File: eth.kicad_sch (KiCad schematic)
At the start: 58 parts, among them U1901 KSZ9131RNXC, Y1901 Resonator_25MHz_ECX-1247Q

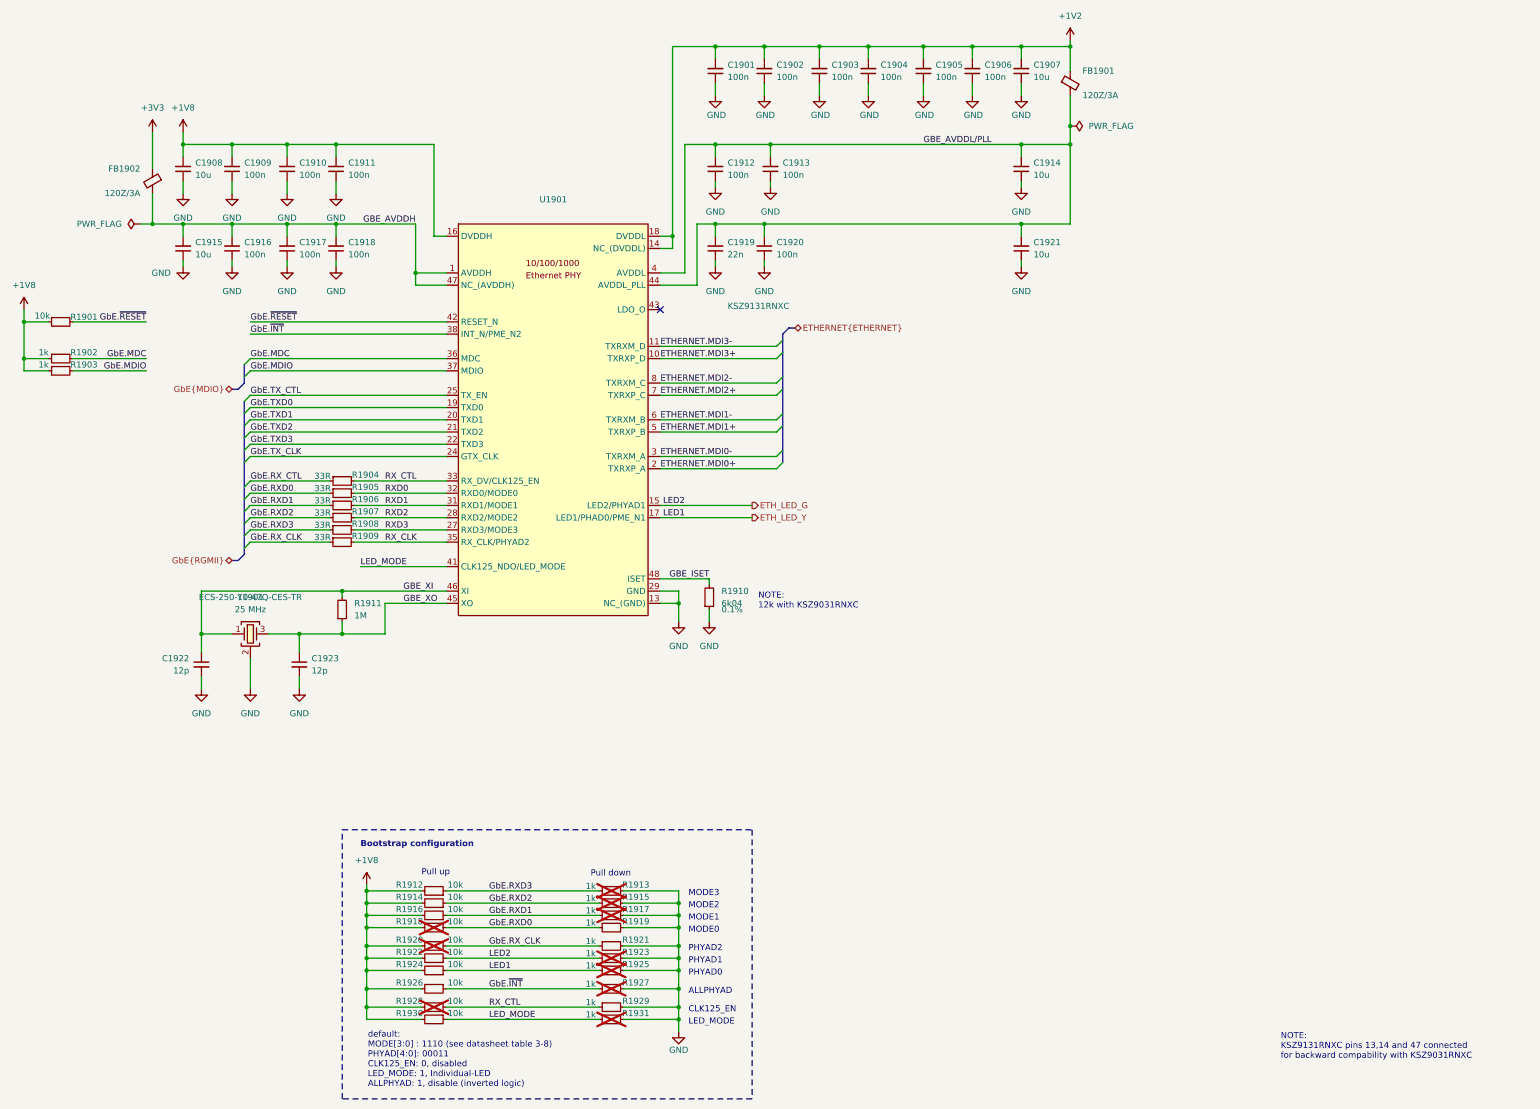
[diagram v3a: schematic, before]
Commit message: [#100282] Clear ERC
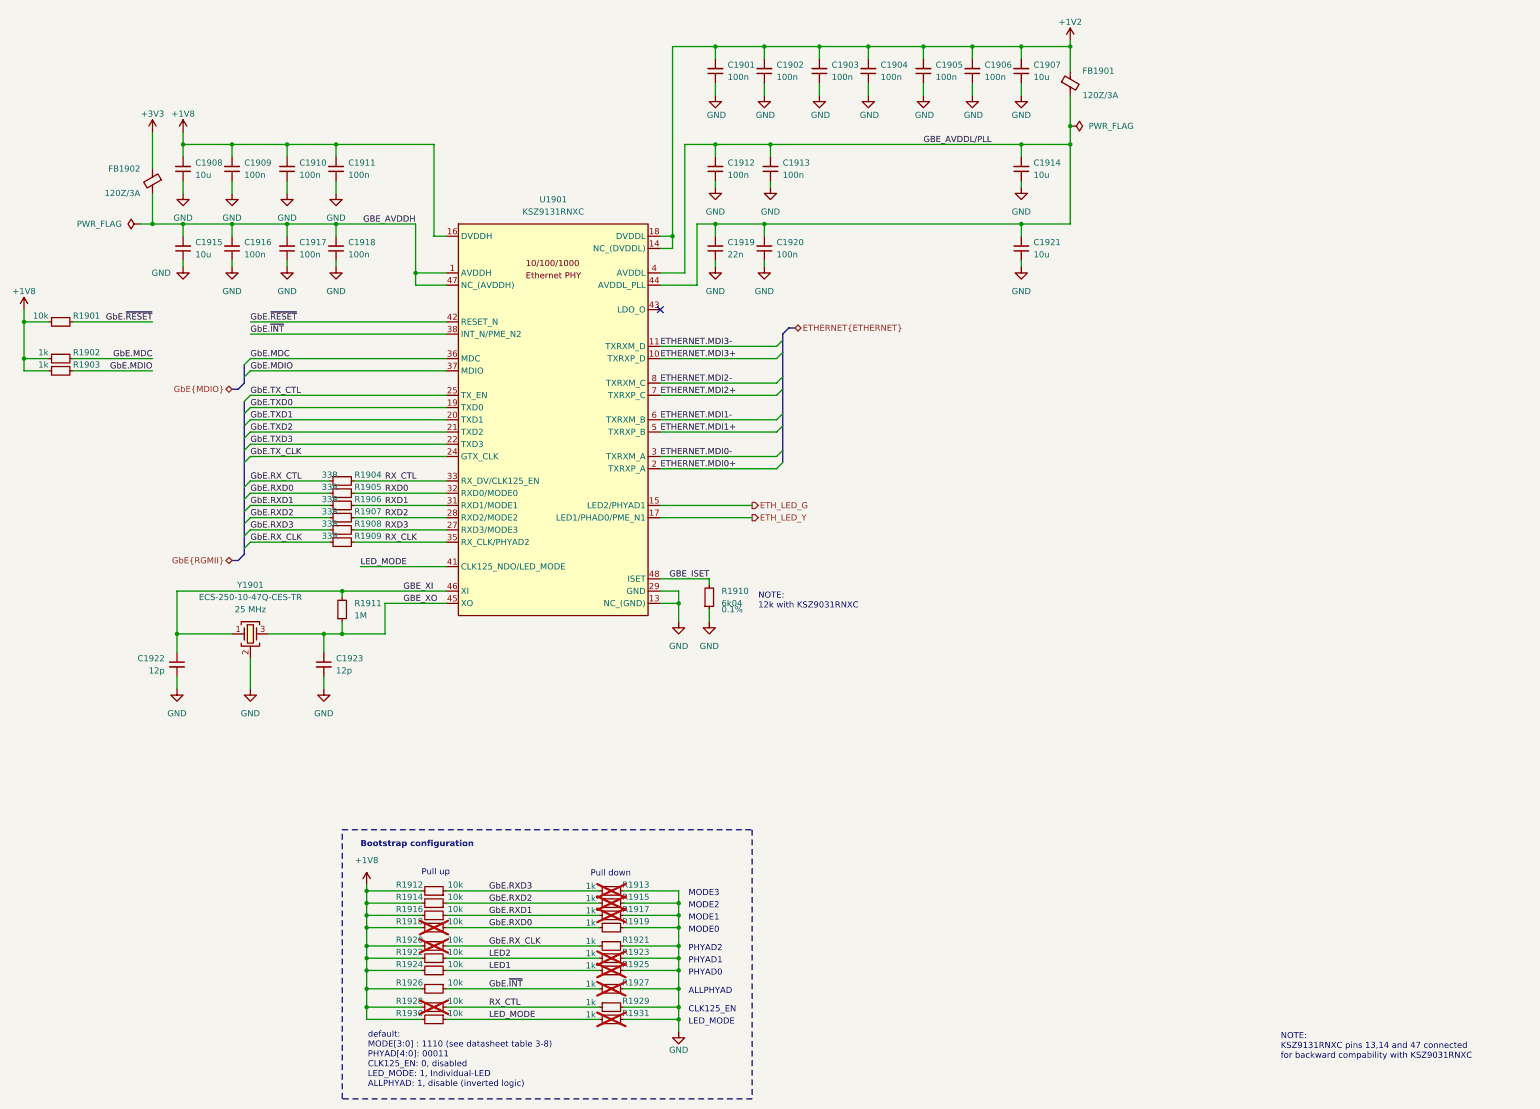
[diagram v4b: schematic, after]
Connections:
- net ETH_LED_G: no longer R1922.1, R1923.1
- net ETH_LED_Y: no longer R1924.1, R1925.1
- new net LED1: R1924.1, R1925.1
- new net LED2: R1922.1, R1923.1
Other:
- moved on the sheet: C1922, C1923

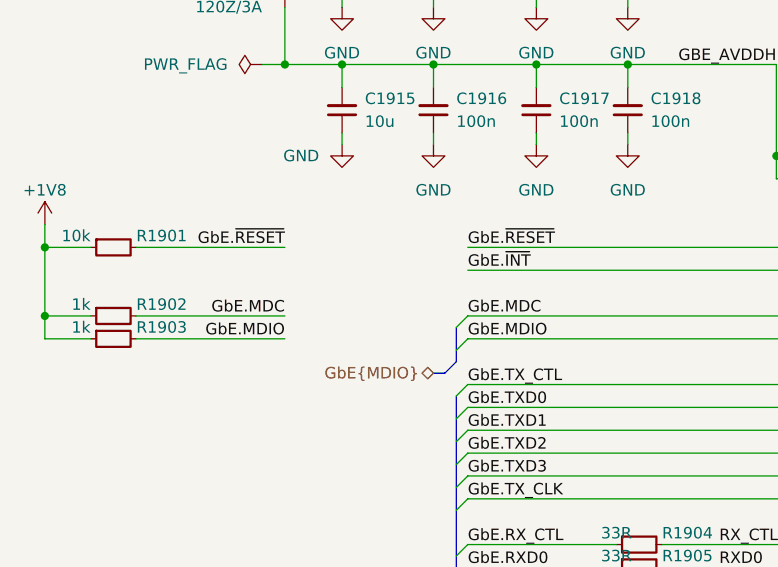
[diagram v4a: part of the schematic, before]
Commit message: [#100282] Connect ETH PHY reset to SOM
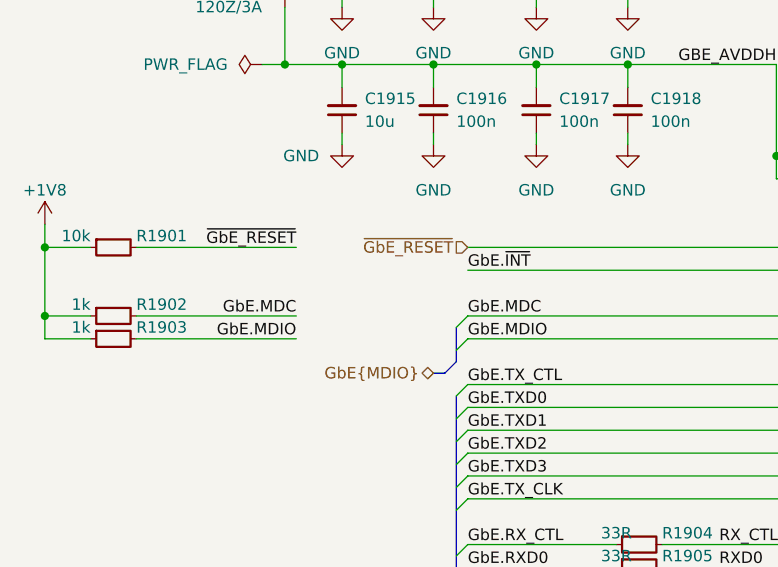
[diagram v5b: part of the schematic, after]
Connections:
- net GbE.~{RESET} renamed ~{GbE_RESET}
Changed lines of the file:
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@@
 	(wire
 		(pts
-			(xy 128.27 107.95) (xy 111.76 107.95)
+			(xy 129.54 107.95) (xy 111.76 107.95)
 		)
 		(stroke
@@
 	(wire
 		(pts
-			(xy 128.27 105.41) (xy 111.76 105.41)
+			(xy 129.54 105.41) (xy 111.76 105.41)
 		)
 		(stroke
@@
 	(wire
 		(pts
-			(xy 128.27 97.79) (xy 111.76 97.79)
+			(xy 129.54 97.79) (xy 111.76 97.79)
 		)
 		(stroke
@@
 	)
 	(label "GbE.MDIO"
-		(at 128.27 107.95 180)
+		(at 129.54 107.95 180)
 		(effects
 			(font
@@
 		)
 	)
+	(label "~{GbE_RESET}"
+		(at 129.54 97.79 180)
+		(effects
+			(font
+				(size 1.27 1.27)
+			)
+			(justify right bottom)
+		)
+	)
 	(label "GbE.RXD3"
 		(at 148.59 140.97 0)
@@
 		)
 	)
-	(label "GbE.~{RESET}"
-		(at 128.27 97.79 180)
-		(effects
-			(font
-				(size 1.27 1.27)
-			)
-			(justify right bottom)
-		)
-	)
 	(label "RXD3"
 		(at 176.53 140.97 0)
@@
 		)
 	)
-	(label "GbE.~{RESET}"
-		(at 148.59 97.79 0)
-		(effects
-			(font
-				(size 1.27 1.27)
-			)
-			(justify left bottom)
-		)
-	)
 	(label "GbE.RX_CTL"
 		(at 148.59 130.81 0)
@@
 	)
 	(label "GbE.MDC"
-		(at 128.27 105.41 180)
+		(at 129.54 105.41 180)
 		(effects
 			(font
@@
 		(effects
 			(font
+				(size 1.27 1.27)
+			)
+			(justify right)
+		)
+	)
+	(hierarchical_label "~{GbE_RESET}"
+		(shape input)
+		(at 148.59 97.79 180)
+		(effects
+			(font

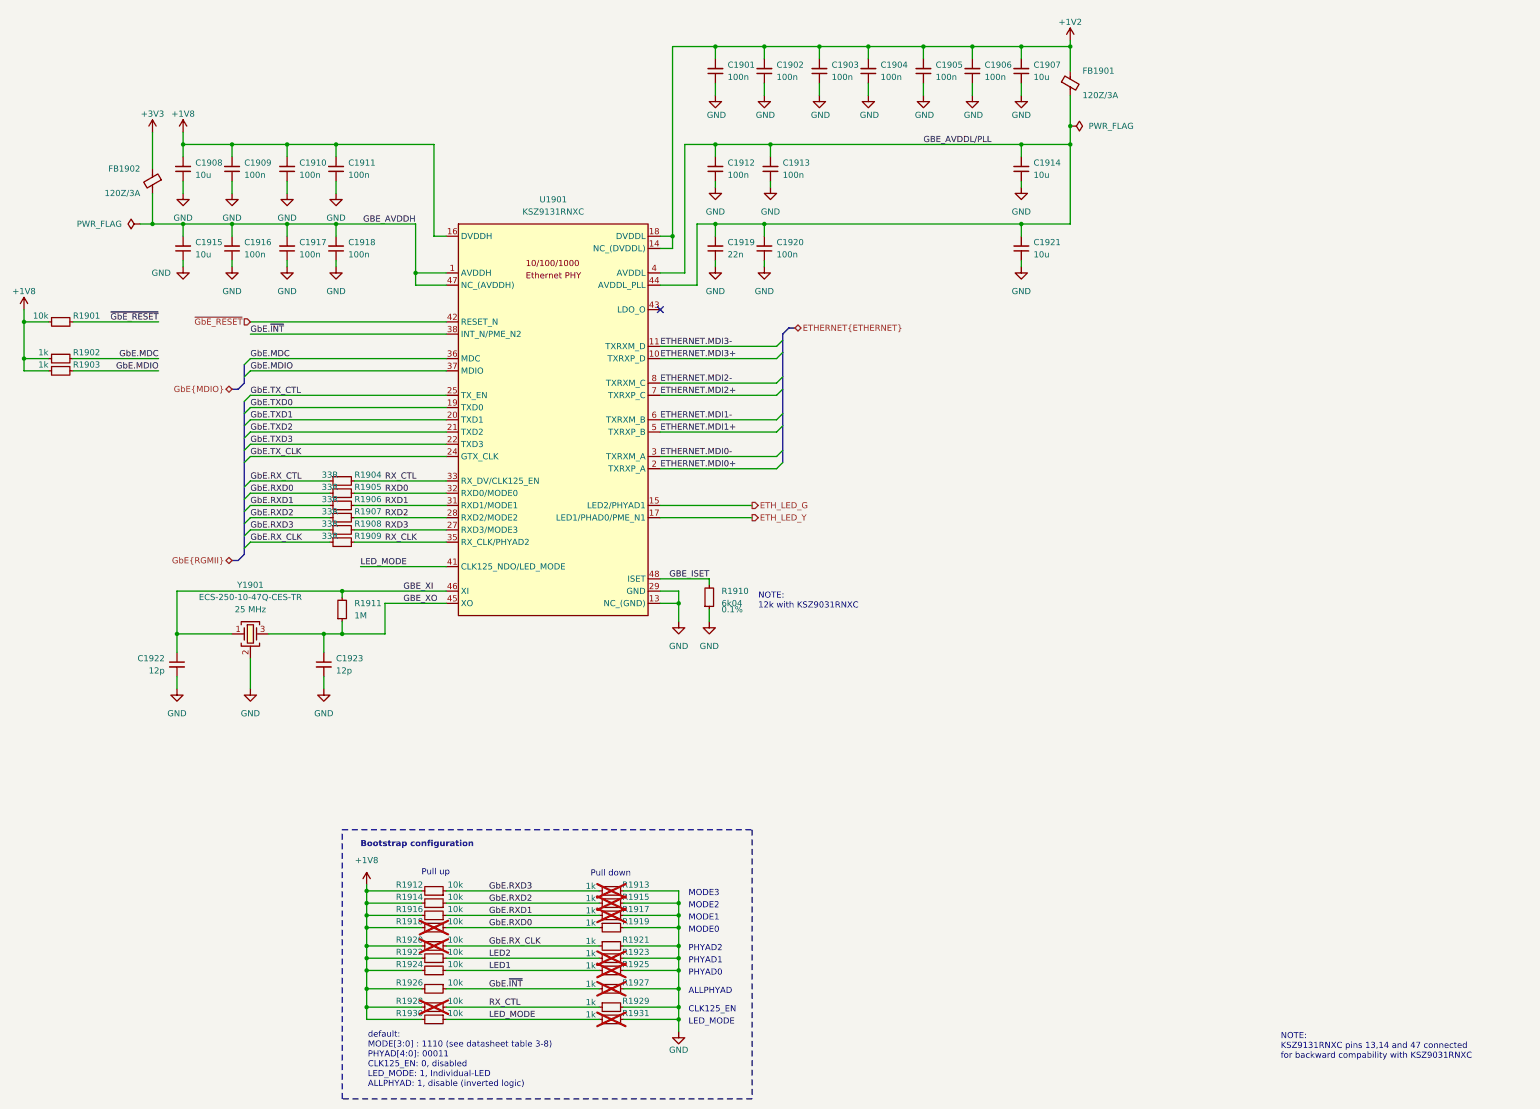
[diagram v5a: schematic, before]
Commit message: [#100282] Fix overlaping graphics, add schematic sheet names on them
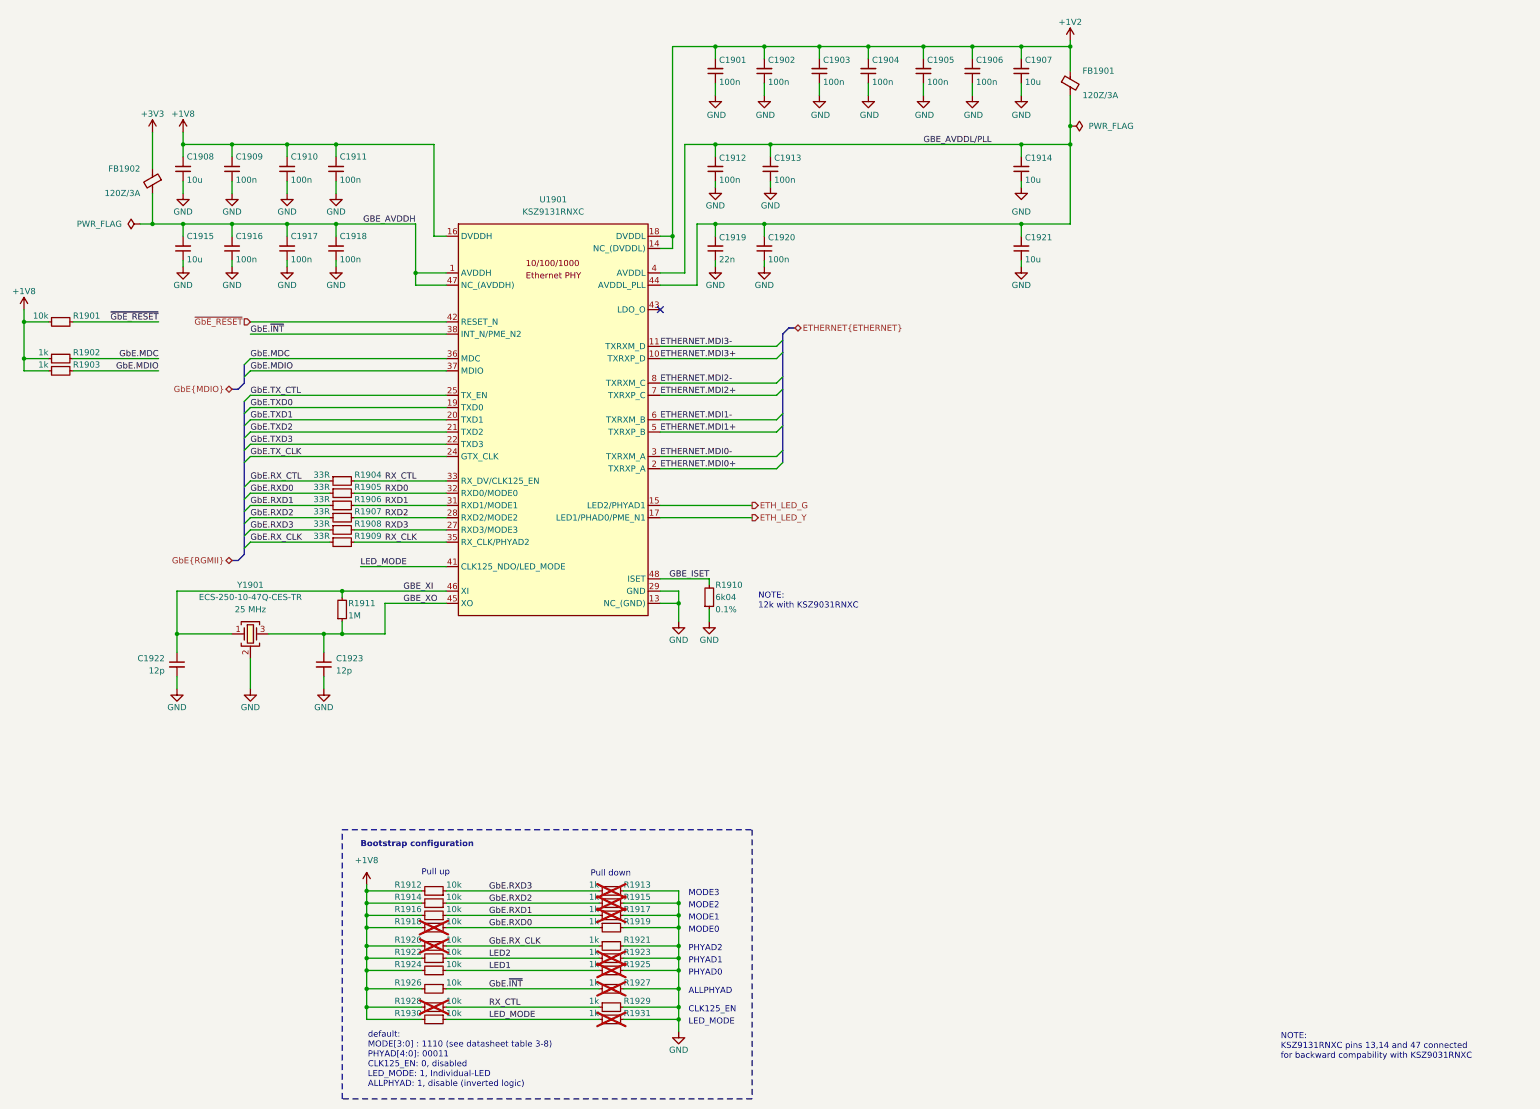
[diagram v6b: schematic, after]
